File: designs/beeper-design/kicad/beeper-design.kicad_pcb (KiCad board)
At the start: 4 copper layers, 26 x 19 mm, 90 parts

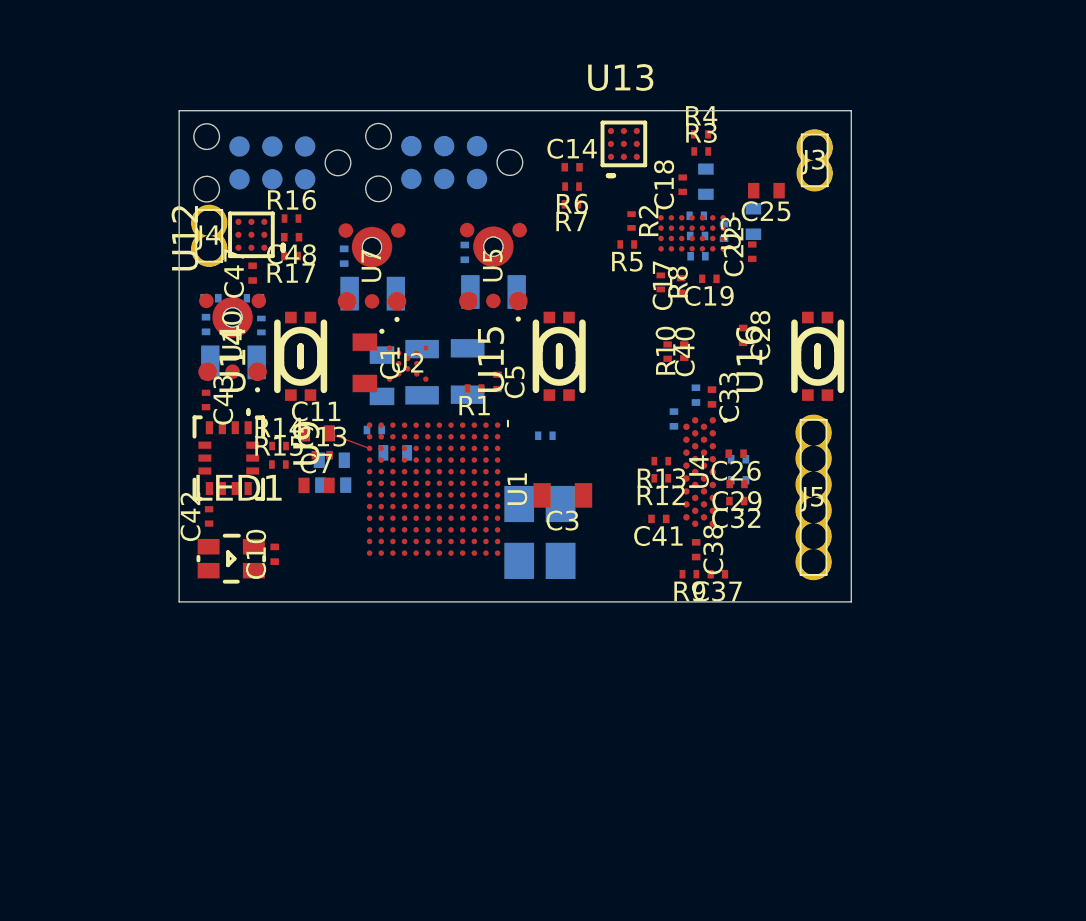
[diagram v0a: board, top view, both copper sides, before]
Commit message: fixed BGA ball landpattern
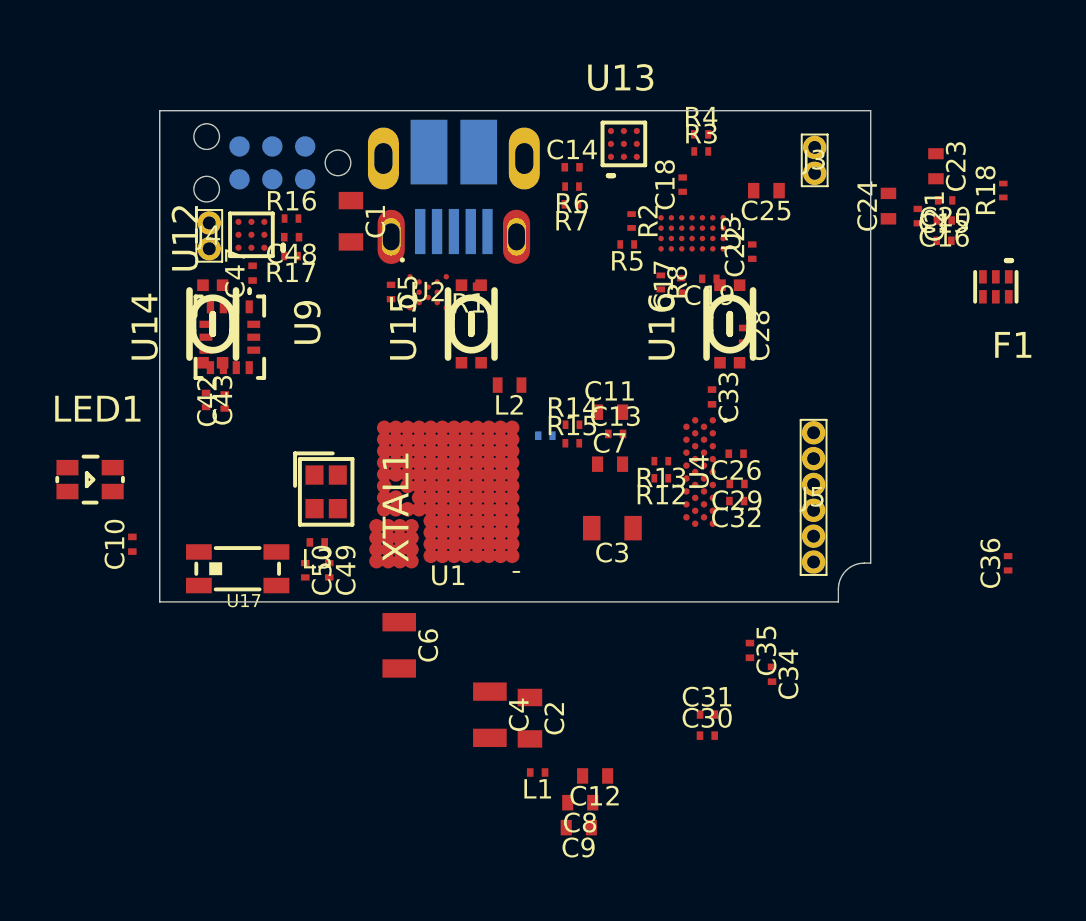
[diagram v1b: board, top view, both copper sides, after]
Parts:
- removed C37, C40, C45: 100p, beeper-design:Pkg0201_1
- removed C38, C39, C41, C44, C46: 1u, beeper-design:Pkg0201_4
- removed J2: ~, beeper-design:TC2030_IDC_NL_FOOTPRINT
- removed R10, R11, R9: 47K, beeper-design:Pkg0201_5
- removed U10, U5, U7: ~, beeper-design:LP_7
- removed U11, U6, U8: ~, beeper-design:Pkg0805
- removed X1: ~, beeper-design:XTAL_TSX_3225
- added C49: 1p, beeper-design:Pkg0201_1, F.Cu at (132.3, 116.3)
- added C50: 1p, beeper-design:Pkg0201_1, F.Cu at (131.4, 116.3)
- added F1: ~, beeper-design:SON_6_L1_5_W1_0_P0_50_BL, F.Cu at (158.1, 105.3)
- added J6: ~, beeper-design:AMPHENOL_10103594_0001LF, B.Cu at (137.1, 100.3)
- added L3: 1n, beeper-design:Pkg0201_2, F.Cu at (131.8, 115.2)
- added R18: 100K, beeper-design:Pkg0201_5, F.Cu at (158.4, 101.6)
- added U17: ~, beeper-design:Pkg_2450AT18D0100_STD_R_1, F.Cu at (128.8, 116.2)
- added XTAL1: ~, beeper-design:CRYSTAL_SMD_4P_L2_0_W1_6_BL_1, F.Cu at (132.1, 113.1)
- C12, C15, C16, C2, C20, C21, C23, C24, C30, C31, C34, C35, C8, C9, L1, L2: moved to F.Cu
- C36: value 1u -> 100n; footprint beeper-design:Pkg0201_4 -> beeper-design:Pkg0201_1; moved to F.Cu
- C4, C6: footprint beeper-design:Pkg0805_1 -> beeper-design:Pkg0805; moved to F.Cu
- U1: footprint beeper-design:LP_1 -> beeper-design:LP_5
- U12: footprint beeper-design:LP_5 -> beeper-design:LP_6
- U14, U15, U16: footprint beeper-design:LP_6 -> beeper-design:LP_2
- U4: footprint beeper-design:LP_2 -> beeper-design:LP
- U9: footprint beeper-design:LP -> beeper-design:LP_1
- moved C36 24.2 mm to (158.6, 116.0), turned to 180 degrees
- moved C12 17.1 mm to (142.6, 124.2), turned to 270 degrees
- moved C8 16.4 mm to (142.0, 125.3), turned to 270 degrees
- moved C9 16.3 mm to (142.0, 126.2), turned to 270 degrees
- moved L1 14.7 mm to (140.4, 124.1), turned to 270 degrees
- moved C2 14.4 mm to (140.1, 122.0)
- moved C4 13.5 mm to (138.5, 121.9)
- moved C11 11.4 mm to (143.2, 110.2)
- moved R14 11.4 mm to (141.7, 110.6)
- moved C13 11.4 mm to (143.4, 111.0)
- moved R15 11.4 mm to (141.7, 111.4)
- moved C7 11.4 mm to (143.2, 112.2)
- moved C6 10.9 mm to (135.0, 119.2)
- moved C34 10.6 mm to (149.4, 120.3)
- moved C35 10.1 mm to (148.6, 119.4)
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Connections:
- net D11 renamed VBUS
- net VSYS renamed VDDSYS
- net mcu-i3c_sda renamed qsen-i3c_sda
- net mcu_dbg-m33_swdio renamed mcu_mcu-dbg-m33_swdio
- net qsen-i3c_scl renamed mcu-i3c_scl
- C36 pad 1: GND -> SHIELD
- C36 pad 2: MICBIAS1 -> GND
- J1 pad 3: mcu_conn-reset_reset -> mcu_mcu-uart_rx
- J1 pad 6: (no net) -> mcu_conn-uart_tx
- R13 pad 1: codec-i2c_scl -> mcu-codec-i2c_scl
- R17 pad 1: drv-i2c_scl -> mcu-hap-i2c_scl
- U1 pad A10: (no net) -> RFIOP
- U1 pad A4: mcu-wpwr2_gpio -> mcu-but2_gpio
- U1 pad A5: mcu-wpwr3_gpio -> drv-i2c_sda
- U1 pad B1: mcu-wpwr0_gpio -> mcu-but0_gpio
- U1 pad B10: mcu_conn-reset_reset -> (no net)
- U1 pad B2: mcu-wpwr1_gpio -> mcu-but1_gpio
- U1 pad D1: (no net) -> mcu-hap1_gpio
- U1 pad D2: codec-i2c_sda -> mcu-codec-i2c_scl
- U1 pad D3: drv-i2c_scl -> mcu_mcu-uart_rx
- U1 pad D7: mcu_dbg-snc_swdclk -> (no net)
- U1 pad D8: mcu_dbg-snc_swdio -> (no net)
- U1 pad E2: codec-i2c_scl -> mcu_conn-uart_tx
- U1 pad E3: (no net) -> mcu-wpwr0_gpio
- U1 pad E4: mcu-hap0_gpio -> mcu-wpwr2_gpio
- U1 pad E6: mcu-hap1_gpio -> mcu-wpwr3_gpio
- U1 pad F1: mcu-but2_gpio -> D+
- U1 pad F2: (no net) -> mcu-hap0_gpio
- U1 pad G1: drv-i2c_sda -> D-
- U1 pad H11: mcu-but1_gpio -> mcu-hap-i2c_scl
- U1 pad H12: mcu-but0_gpio -> codec-i2c_sda
- U1 pad J9: (no net) -> mcu-wpwr1_gpio
- U1 pad M9: VAD -> (no net)
- U12 pad C1: drv-i2c_scl -> mcu-hap-i2c_scl
- U4 pad A15: MICBIAS1 -> (no net)
- U4 pad A17: MICBIAS2 -> (no net)
- U4 pad C17: MIC1_P -> (no net)
- U4 pad D16: MIC2_P -> (no net)
- U4 pad D8: codec-i2c_scl -> mcu-codec-i2c_scl
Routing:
- net VDDSYS: track 1.67 -> 0.00 mm
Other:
- board size 26 x 19 mm -> 27.5 x 19 mm
- net class Default: clearance 0.05 -> 0.09; trace_width 0.05 -> 0.09; via_dia 0.01 -> 0.015; via_drill 0.1 -> 0.15

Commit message: fixed up 3D flex conn
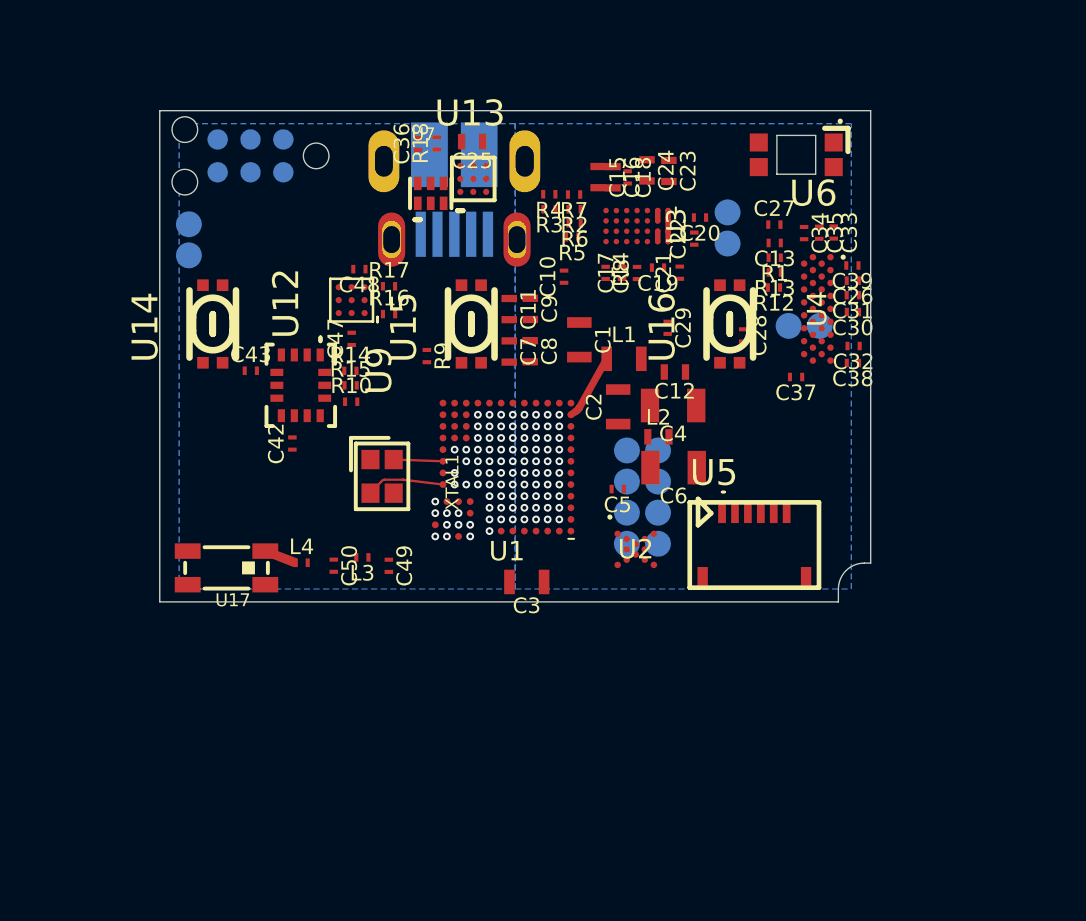
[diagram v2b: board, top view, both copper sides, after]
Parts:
- removed F1: ~, beeper-design:SON_6_L1_5_W1_0_P0_50_BL
- removed J3, J4: ~, beeper-design:PIN_GRID_1
- removed J5: ~, beeper-design:PIN_GRID
- removed LED1: ~, beeper-design:LED_SMD_4P_L1_6_W1_5_TJ_S1615SW6TWMLCCYRGB_A5
- added ?: , beeper-design:dummy0, F.Cu at (145.0, 102.6)
- added ?: , beeper-design:dummy1, F.Cu at (145.4, 103.0)
- added ?: , beeper-design:dummy2, F.Cu at (145.4, 102.6)
- added ?: , beeper-design:dummy3, F.Cu at (145.4, 103.4)
- added ?: , beeper-design:dummy4, F.Cu at (141.7, 110.2)
- added ?: , beeper-design:dummy5, F.Cu at (130.4, 115.8)
- added ?: , beeper-design:dummy6, F.Cu at (145.0, 103.4)
- added C37: 1u, beeper-design:Pkg0201_42, F.Cu at (150.4, 108.8)
- added C38: 1u, beeper-design:Pkg0201_4, F.Cu at (152.6, 108.3)
- added C39: 1u, beeper-design:Pkg0201_26, F.Cu at (152.5, 104.5)
- added L4: 1n, beeper-design:Pkg0201_16, F.Cu at (131.2, 116.0)
- added R10: 0R, beeper-design:Pkg0201_41, F.Cu at (133.2, 109.8)
- added R9: 0R, beeper-design:Pkg0201_32, F.Cu at (136.1, 108.0)
- added TP1: ~, beeper-design:SMD_TESTPT, B.Cu at (126.9, 104.1)
- added TP10: ~, beeper-design:SMD_TESTPT, B.Cu at (145.0, 114.0)
- added TP11: ~, beeper-design:SMD_TESTPT, B.Cu at (143.8, 115.3)
- added TP12: ~, beeper-design:SMD_TESTPT, B.Cu at (145.0, 115.3)
- added TP13: ~, beeper-design:SMD_TESTPT, B.Cu at (147.7, 103.6)
- added TP14: ~, beeper-design:SMD_TESTPT, B.Cu at (147.7, 102.4)
- added TP2: ~, beeper-design:SMD_TESTPT, B.Cu at (126.9, 102.9)
- added TP3: ~, beeper-design:SMD_TESTPT, B.Cu at (151.3, 106.8)
- added TP4: ~, beeper-design:SMD_TESTPT, B.Cu at (150.1, 106.8)
- added TP5: ~, beeper-design:SMD_TESTPT, B.Cu at (145.0, 111.6)
- added TP6: ~, beeper-design:SMD_TESTPT, B.Cu at (145.0, 112.8)
- added TP7: ~, beeper-design:SMD_TESTPT, B.Cu at (143.8, 112.8)
- added TP8: ~, beeper-design:SMD_TESTPT, B.Cu at (143.8, 114.0)
- added TP9: ~, beeper-design:SMD_TESTPT, B.Cu at (143.8, 111.6)
- added U5: ~, beeper-design:LP_6, F.Cu at (148.8, 113.7)
- added U6: ~, beeper-design:LP_5, F.Cu at (150.4, 100.2)
- added U7: ~, beeper-design:SON_6_L1_5_W1_0_P0_50_BL, F.Cu at (136.2, 101.7)
- C10: footprint beeper-design:Pkg0201_4 -> beeper-design:Pkg0201_18
- C11: footprint beeper-design:Pkg0402_1 -> beeper-design:Pkg0402_6
- C12: footprint beeper-design:Pkg0402_1 -> beeper-design:Pkg0402_5
- C13: footprint beeper-design:Pkg0201_4 -> beeper-design:Pkg0201_34
- C14: footprint beeper-design:Pkg0201_4 -> beeper-design:Pkg0201_2
- C15: footprint beeper-design:Pkg0201_4 -> beeper-design:Pkg0402_10
- C16: footprint beeper-design:Pkg0201_4 -> beeper-design:Pkg0402_4
- C17: footprint beeper-design:Pkg0201_1 -> beeper-design:Pkg0201_21
- C18: footprint beeper-design:Pkg0201_1 -> beeper-design:Pkg0201_33
- C19: footprint beeper-design:Pkg0201_1 -> beeper-design:Pkg0201_43
- C2: footprint beeper-design:Pkg0603 -> beeper-design:Pkg0603_1
- C20: footprint beeper-design:Pkg0201_1 -> beeper-design:Pkg0201_6
- C21: footprint beeper-design:Pkg0201_1 -> beeper-design:Pkg0201_19
- C22: footprint beeper-design:Pkg0201_1 -> beeper-design:Pkg0201_30
- C23: footprint beeper-design:Pkg0402_1 -> beeper-design:Pkg0402_8
- C25: footprint beeper-design:Pkg0402_2 -> beeper-design:Pkg0402
- C26: footprint beeper-design:Pkg0201_4 -> beeper-design:Pkg0201_44
- C27: footprint beeper-design:Pkg0201_1 -> beeper-design:Pkg0201_5; moved to F.Cu
- C28: footprint beeper-design:Pkg0201_4 -> beeper-design:Pkg0201_17
- C29: footprint beeper-design:Pkg0201_4 -> beeper-design:Pkg0201_29
- C3: footprint beeper-design:Pkg0603 -> beeper-design:Pkg0603_2
- C30: footprint beeper-design:Pkg0201_4 -> beeper-design:Pkg0201_15
- C31: footprint beeper-design:Pkg0201_4 -> beeper-design:Pkg0201_28
- C32: footprint beeper-design:Pkg0201_4 -> beeper-design:Pkg0201_40
- C33: footprint beeper-design:Pkg0201_4 -> beeper-design:Pkg0201_3
- C34: footprint beeper-design:Pkg0201_4 -> beeper-design:Pkg0201_14
- C35: footprint beeper-design:Pkg0201_4 -> beeper-design:Pkg0201_38
- C36: footprint beeper-design:Pkg0201_1 -> beeper-design:Pkg0201_31
- C4: footprint beeper-design:Pkg0805 -> beeper-design:Pkg0805_1
- C42: footprint beeper-design:Pkg0201_1 -> beeper-design:Pkg0201_45
- C43: footprint beeper-design:Pkg0201_1 -> beeper-design:Pkg0201_8
- C47: footprint beeper-design:Pkg0201_4 -> beeper-design:Pkg0201_10
- C48: footprint beeper-design:Pkg0201_4 -> beeper-design:Pkg0201_22
- C49: footprint beeper-design:Pkg0201_1 -> beeper-design:Pkg0201_39
- C5: footprint beeper-design:Pkg0201_1 -> beeper-design:Pkg0201_7
- C50: footprint beeper-design:Pkg0201_1 -> beeper-design:Pkg0201_9
- C7: footprint beeper-design:Pkg0402_1 -> beeper-design:Pkg0402_7
- C8: footprint beeper-design:Pkg0402_1 -> beeper-design:Pkg0402_9
- C9: footprint beeper-design:Pkg0402_1 -> beeper-design:Pkg0402_3
- L1: footprint beeper-design:Pkg0201_2 -> beeper-design:Pkg0603_3
- L2: footprint beeper-design:Pkg0402 -> beeper-design:Pkg0402_1
- L3: footprint beeper-design:Pkg0201_2 -> beeper-design:Pkg0201_1
- R1: footprint beeper-design:Pkg0201_5 -> beeper-design:Pkg0201_25
- R12, R13: footprint beeper-design:Pkg0201_5 -> beeper-design:Pkg0201_27
- R14, R15: footprint beeper-design:Pkg0201_5 -> beeper-design:Pkg0201_12
- R16, R17: footprint beeper-design:Pkg0201_5 -> beeper-design:Pkg0201_37
- R18: footprint beeper-design:Pkg0201_5 -> beeper-design:Pkg0201_20
- R2: footprint beeper-design:Pkg0201_5 -> beeper-design:Pkg0201_13
- R3: footprint beeper-design:Pkg0201 -> beeper-design:Pkg0201_24
- R4: footprint beeper-design:Pkg0201_3 -> beeper-design:Pkg0201_36
- R5: footprint beeper-design:Pkg0201_5 -> beeper-design:Pkg0201
- R6: footprint beeper-design:Pkg0201_5 -> beeper-design:Pkg0201_11
- R7: footprint beeper-design:Pkg0201_5 -> beeper-design:Pkg0201_23
- R8: footprint beeper-design:Pkg0201 -> beeper-design:Pkg0201_35
- U1: footprint beeper-design:LP_5 -> beeper-design:LP_1
- U12: footprint beeper-design:LP_6 -> beeper-design:LP
- U13: footprint beeper-design:LP_3 -> beeper-design:LP_7
- U14, U15, U16: footprint beeper-design:LP_2 -> beeper-design:LP_3
- U3: footprint beeper-design:LP_4 -> beeper-design:LP_8
- U4: footprint beeper-design:LP -> beeper-design:LP_4
- U9: footprint beeper-design:LP_1 -> beeper-design:LP_2
- moved C36 28.0 mm to (135.7, 99.8)
- moved R18 22.0 mm to (136.5, 99.8)
- moved C9 20.2 mm to (140.1, 106.2), turned to 0 degrees
- moved C10 19.6 mm to (141.4, 104.9)
- moved C8 17.6 mm to (140.1, 107.8), turned to 0 degrees
- moved C30 17.3 mm to (152.6, 106.3), turned to 270 degrees
- moved C31 17.2 mm to (152.6, 105.6), turned to 270 degrees
- moved C34 17.1 mm to (150.7, 103.2)
- moved C35 16.4 mm to (151.3, 103.2)
- moved L1 16.3 mm to (143.7, 108.1), turned to 90 degrees
- moved C12 15.9 mm to (145.7, 108.6)
- moved C4 13.9 mm to (145.6, 109.9), turned to 270 degrees
- moved C15 13.6 mm to (142.7, 101.1), turned to 0 degrees
- moved C16 12.9 mm to (143.3, 101.1), turned to 0 degrees
- moved U2 12.8 mm to (144.2, 115.5)
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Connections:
- net RFIOP renamed RF1
- net SHIELD renamed rid_p1
- net VDD1P2 renamed V12
- net VDD1P4 renamed V14RF
- net VDD1P8F renamed V18F
- net VDD1P8P renamed V18P
- net VDDBAT renamed VBAT
- net VDDBUS renamed mcu_VBUS
- net drv-i2c_sda renamed mcu_hap-i2c_sda
- net mcu-hap-i2c_scl renamed mcu_hap-i2c_scl
- net mcu-i3c_scl renamed board-io_qsen-i3c_scl
- net mcu_mcu-dbg-m33_swdio renamed mcu_dbg-m33_swdio
- net qsen-i3c_sda renamed board-io_qsen-i3c_sda
- C26 pad 2: VDD1P8 -> VDD_A
- C28 pad 2: VDD1P8 -> VDD_A
- C32 pad 2: VDD1P8 -> VDD_A
- C4 pad 2: VDD1P8 -> VDDSYS
- C42 pad 2: VDD1P8 -> VDDSYS
- C43 pad 2: VDD1P8 -> VDDSYS
- C50 pad 1: ant_p1 -> RF2
- J1 pad 3: mcu_mcu-uart_rx -> mcu_conn-uart_rx
- L3 pad 2: ant_p1 -> RF2
- R12 pad 1: codec-i2c_sda -> mcu_c-i2c_sda
- R13 pad 1: mcu-codec-i2c_scl -> mcu_c-i2c_scl
- R5 pad 1: mcu-wpwr0_gpio -> mcu_mcu-wpwr0_gpio
- R6 pad 1: mcu-wpwr1_gpio -> mcu_mcu-wpwr1_gpio
- R7 pad 1: mcu-wpwr3_gpio -> mcu_mcu-wpwr3_gpio
- U1 pad A4: mcu-but2_gpio -> mcu_q-spi_cs
- U1 pad B1: mcu-but0_gpio -> (no net)
- U1 pad B12: (no net) -> mcu_q-spi_sck
- U1 pad B2: mcu-but1_gpio -> (no net)
- U1 pad B6: (no net) -> mcu_mcu-wpwr1_gpio
- U1 pad B7: (no net) -> mcu_hap-gpio1_gpio
- U1 pad D1: mcu-hap1_gpio -> (no net)
- U1 pad D2: mcu-codec-i2c_scl -> mcu_q-spi_sdo
- U1 pad D3: mcu_mcu-uart_rx -> mcu_c-i2c_sda
- U1 pad D7: (no net) -> mcu_mcu-wpwr2_gpio
- U1 pad D8: (no net) -> mcu_mcu-button2_gpio
- U1 pad D9: (no net) -> mcu_hap-gpio0_gpio
- U1 pad E2: mcu_conn-uart_tx -> mcu_c-i2c_scl
- U1 pad E3: mcu-wpwr0_gpio -> (no net)
- U1 pad E4: mcu-wpwr2_gpio -> (no net)
- U1 pad E6: mcu-wpwr3_gpio -> (no net)
- U1 pad E7: (no net) -> mcu_q-spi_sdi
- U1 pad E9: (no net) -> mcu_mcu-wpwr3_gpio
- U1 pad F2: mcu-hap0_gpio -> (no net)
- U1 pad F3: mem-qspi_sdio3 -> mcu_mcu-button0_gpio
- U1 pad F4: mem-qspi_sck -> (no net)
- U1 pad F8: (no net) -> mcu_mcu-button1_gpio
- U1 pad G10: (no net) -> mcu_mcu-wpwr0_gpio
- U1 pad G2: mem-qspi_sdio1 -> (no net)
- U1 pad G3: (no net) -> mcu_mcu-mem_sdio1
- U1 pad G4: (no net) -> mcu_mcu-mem_sdio3
- U1 pad H12: codec-i2c_sda -> mcu_conn-uart_rx
- U1 pad H3: (no net) -> mcu_mcu-mem_sck
- U1 pad H4: mem-qspi_sdio2 -> (no net)
- U1 pad H5: (no net) -> mcu_mcu-mem_sdio2
- U1 pad J3: mem-qspi_cs -> (no net)
- U1 pad J4: (no net) -> mcu_mcu-mem_sdio0
- U1 pad J5: (no net) -> mcu_mcu-mem_cs
- U1 pad J6: mem-qspi_sdio0 -> (no net)
- U1 pad J9: mcu-wpwr1_gpio -> mcu_conn-uart_tx
- U1 pad K2: VDD1P8 -> VDDSYS
- U1 pad L4: LED3 -> board-io_rgb_b
- U1 pad L5: LED1 -> board-io_rgb_r
- U1 pad L6: LED2 -> board-io_rgb_g
- U12 pad A1: mcu-hap0_gpio -> mcu_hap-gpio0_gpio
- U12 pad B1: mcu-hap1_gpio -> mcu_hap-gpio1_gpio
- U14 pad A: mcu-but0_gpio -> mcu_mcu-button0_gpio
- U14 pad A1: mcu-but0_gpio -> mcu_mcu-button0_gpio
- U15 pad A: mcu-but1_gpio -> mcu_mcu-button1_gpio
- U15 pad A1: mcu-but1_gpio -> mcu_mcu-button1_gpio
- U16 pad A: mcu-but2_gpio -> mcu_mcu-button2_gpio
- U16 pad A1: mcu-but2_gpio -> mcu_mcu-button2_gpio
- U17 pad 1: ant_p1 -> RF3
- U2 pad B4: mem-qspi_cs -> mcu_mcu-mem_cs
- U2 pad D2: mem-qspi_sdio3 -> mcu_mcu-mem_sdio3
- U2 pad D4: mem-qspi_sdio1 -> mcu_mcu-mem_sdio1
- U2 pad E3: mem-qspi_sdio0 -> mcu_mcu-mem_sdio0
- U2 pad F2: mem-qspi_sck -> mcu_mcu-mem_sck
- U2 pad F4: mem-qspi_sdio2 -> mcu_mcu-mem_sdio2
- U3 pad F1: mcu-wpwr3_gpio -> mcu_mcu-wpwr3_gpio
- U3 pad F4: mcu-wpwr2_gpio -> mcu_mcu-wpwr2_gpio
- U3 pad G2: mcu-wpwr1_gpio -> mcu_mcu-wpwr1_gpio
- U3 pad G3: mcu-wpwr0_gpio -> mcu_mcu-wpwr0_gpio
- U4 pad A13: (no net) -> SP_N
- U4 pad A15: (no net) -> MICBIAS1
- U4 pad A17: (no net) -> MICBIAS2
- U4 pad B12: (no net) -> SP_P
- U4 pad B14: VDD1P8 -> VDD_A
- U4 pad B16: (no net) -> board-io_codec-pdm_data
- U4 pad B6: VDD1P8 -> VDD_A
- U4 pad B8: (no net) -> VREF
- U4 pad C11: (no net) -> MCLK
- U4 pad C17: (no net) -> board-io_codec-pdm_clk
- U4 pad C5: (no net) -> DATIN
- U4 pad C7: (no net) -> DATOUT
- U4 pad C9: codec-i2c_sda -> mcu_c-i2c_sda
- U4 pad D10: VDD1P8 -> VDD_A
- U4 pad D4: (no net) -> BCLK
- U4 pad D6: (no net) -> WCLK
- U4 pad D8: mcu-codec-i2c_scl -> mcu_c-i2c_scl
- U9 pad 1: (no net) -> mcu_q-spi_sdi
- U9 pad 11: (no net) -> imu_WCLK
- U9 pad 12: (no net) -> mcu_q-spi_cs
- U9 pad 2: (no net) -> TDMOUT
- U9 pad 3: (no net) -> imu_BCLK
- U9 pad 5: VDD1P8 -> VDDSYS
- U9 pad 6: (no net) -> QVAR1
- U9 pad 8: VDD1P8 -> VDDSYS
- U9 pad 9: (no net) -> QVAR2
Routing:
- net GND: track 0.00 -> 4.94 mm, vias 0 -> 19
- net LY: track 0.00 -> 2.35 mm
- net mcu_q-spi_sdo: vias 0 -> 1
- net mcu_q-spi_sdi: vias 0 -> 1
- net mcu_mcu-wpwr3_gpio: vias 0 -> 1
- net mcu_mcu-wpwr2_gpio: vias 0 -> 1
- net mcu_mcu-wpwr1_gpio: vias 0 -> 1
- net mcu_mcu-wpwr0_gpio: vias 0 -> 1
- net mcu_mcu-mem_sdio3: vias 0 -> 1
- net mcu_mcu-mem_sdio2: vias 0 -> 1
- net mcu_mcu-mem_sdio1: vias 0 -> 1
- net mcu_mcu-mem_sdio0: vias 0 -> 1
- net mcu_mcu-mem_sck: vias 0 -> 1
- net mcu_mcu-mem_cs: vias 0 -> 1
- net mcu_mcu-etm_data3: vias 0 -> 1
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- added copper zone on B.Cu, net QVAR1
- added copper zone on B.Cu, net QVAR2
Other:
- outline, holes or cut-outs redrawn
- net class Default: via_dia 0.015 -> 0.0225
- net class RF added: clearance 0.09, trace_width 0.3493, via_dia 0.0225, via_drill 0.15
